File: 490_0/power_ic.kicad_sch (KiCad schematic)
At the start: 35 parts, among them J11 USB3_A_Stacked, U11 TPS2560DRCR, U19 ECMF04-4HSWM10, U20 ECMF04-4HSWM10, U3 TUSB7320RKMR, X2 ECS-480-18-33-JGN-TR

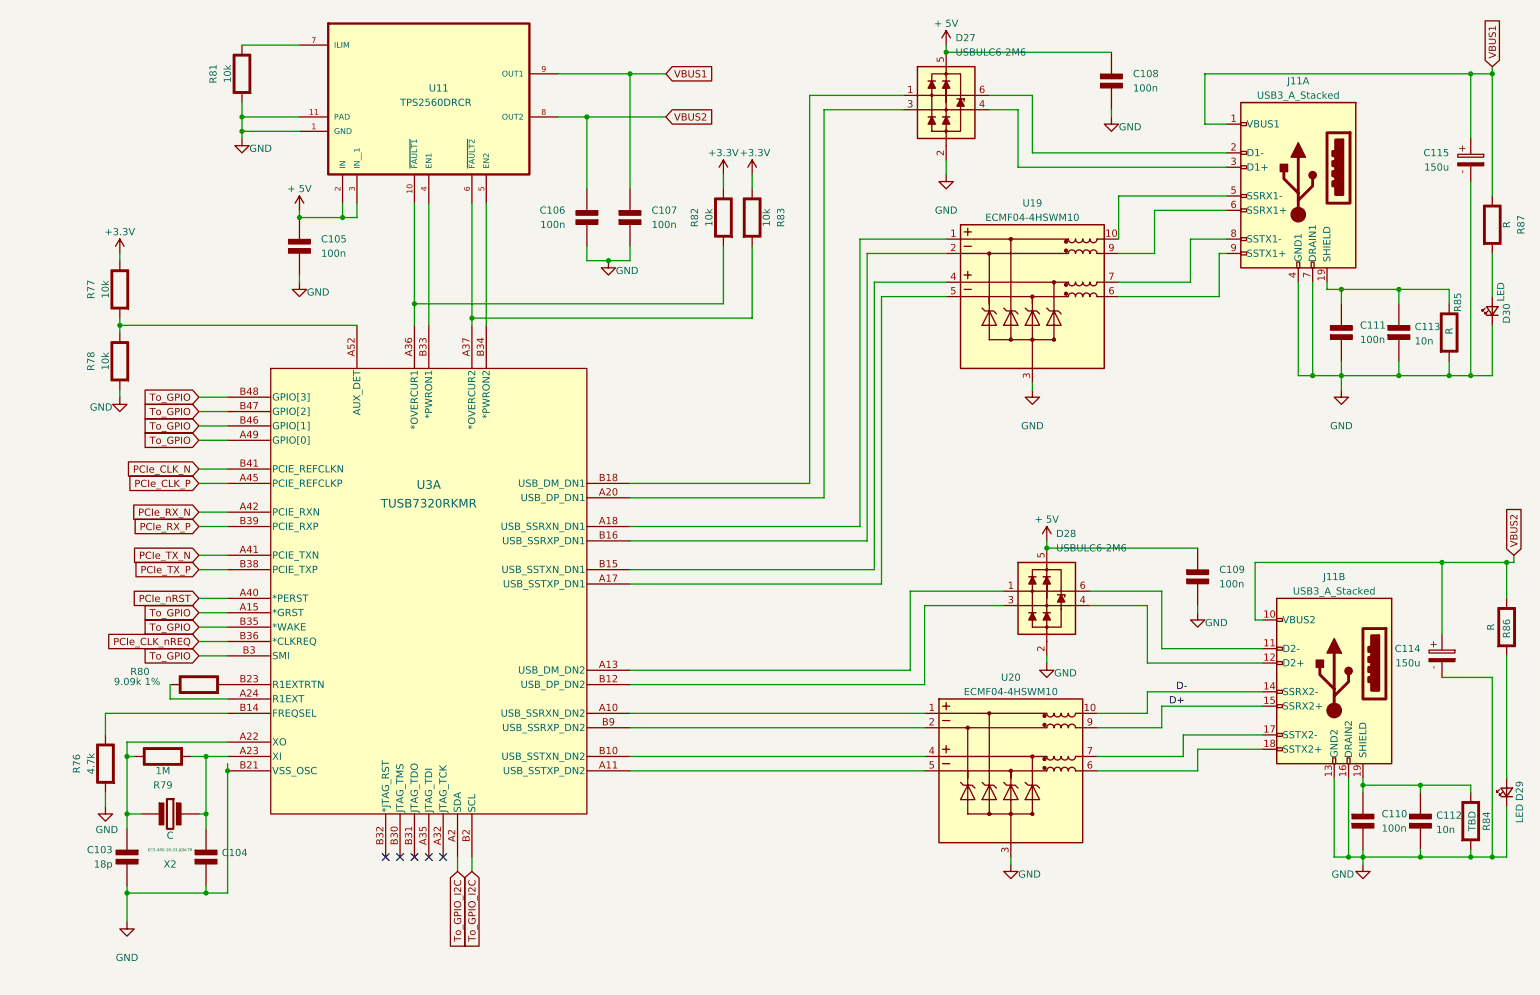
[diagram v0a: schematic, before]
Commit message: US letter format
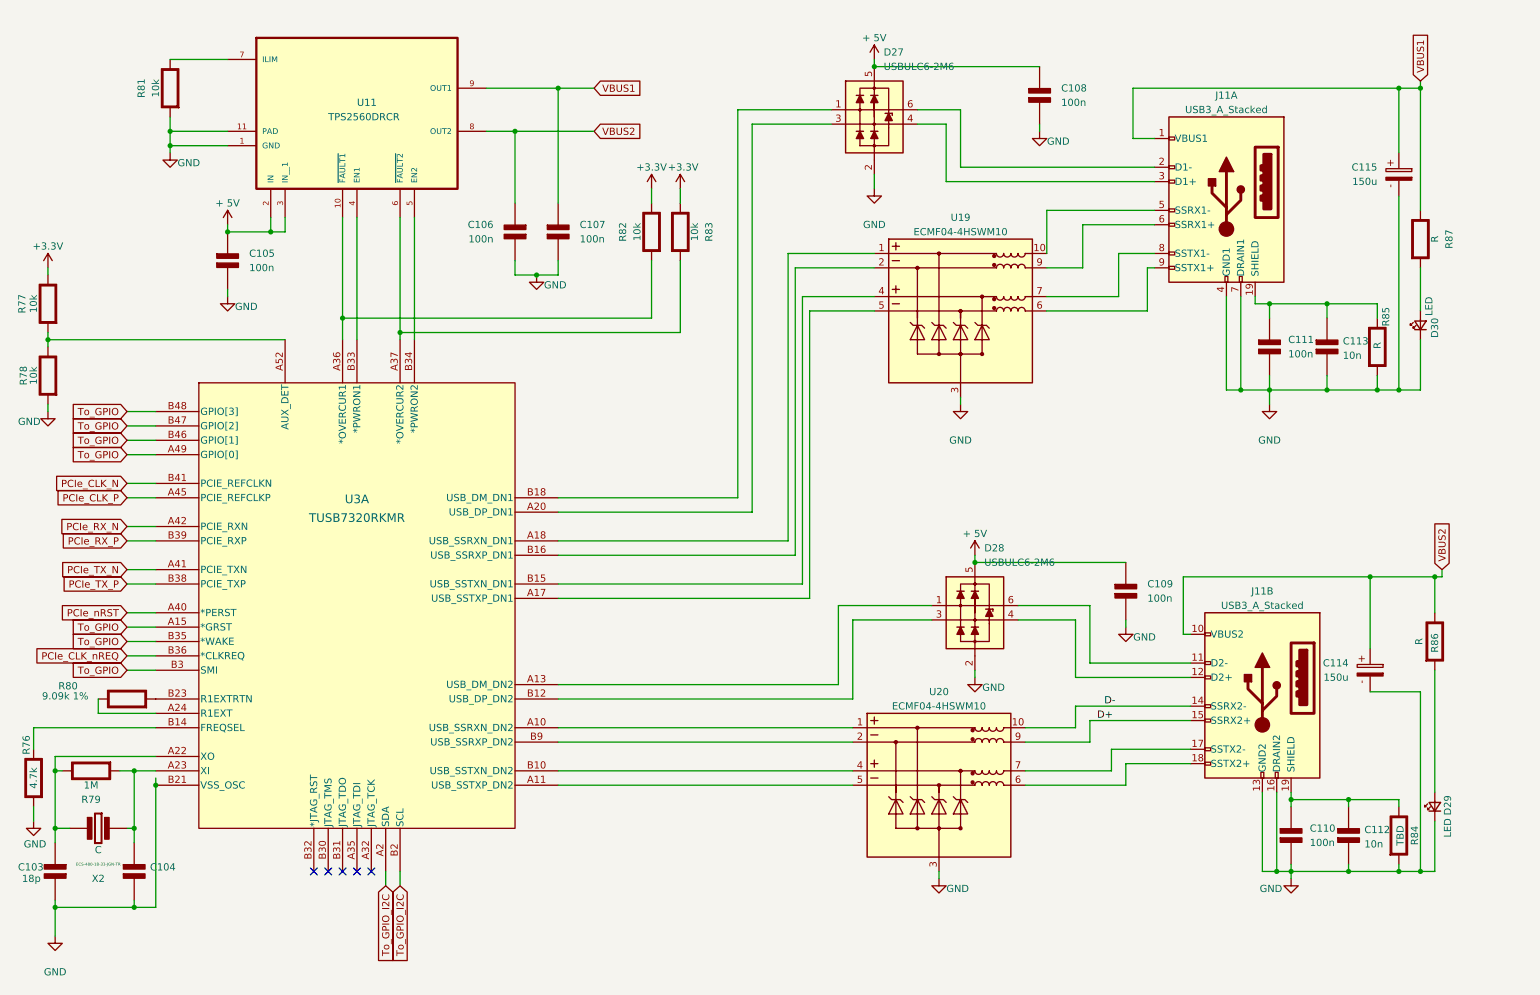
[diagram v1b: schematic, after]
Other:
- moved on the sheet: C103, C104, C105, C106, C107, C108, C109, C110, C111, C112, C113, C114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

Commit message: Changed some local labels to the right format
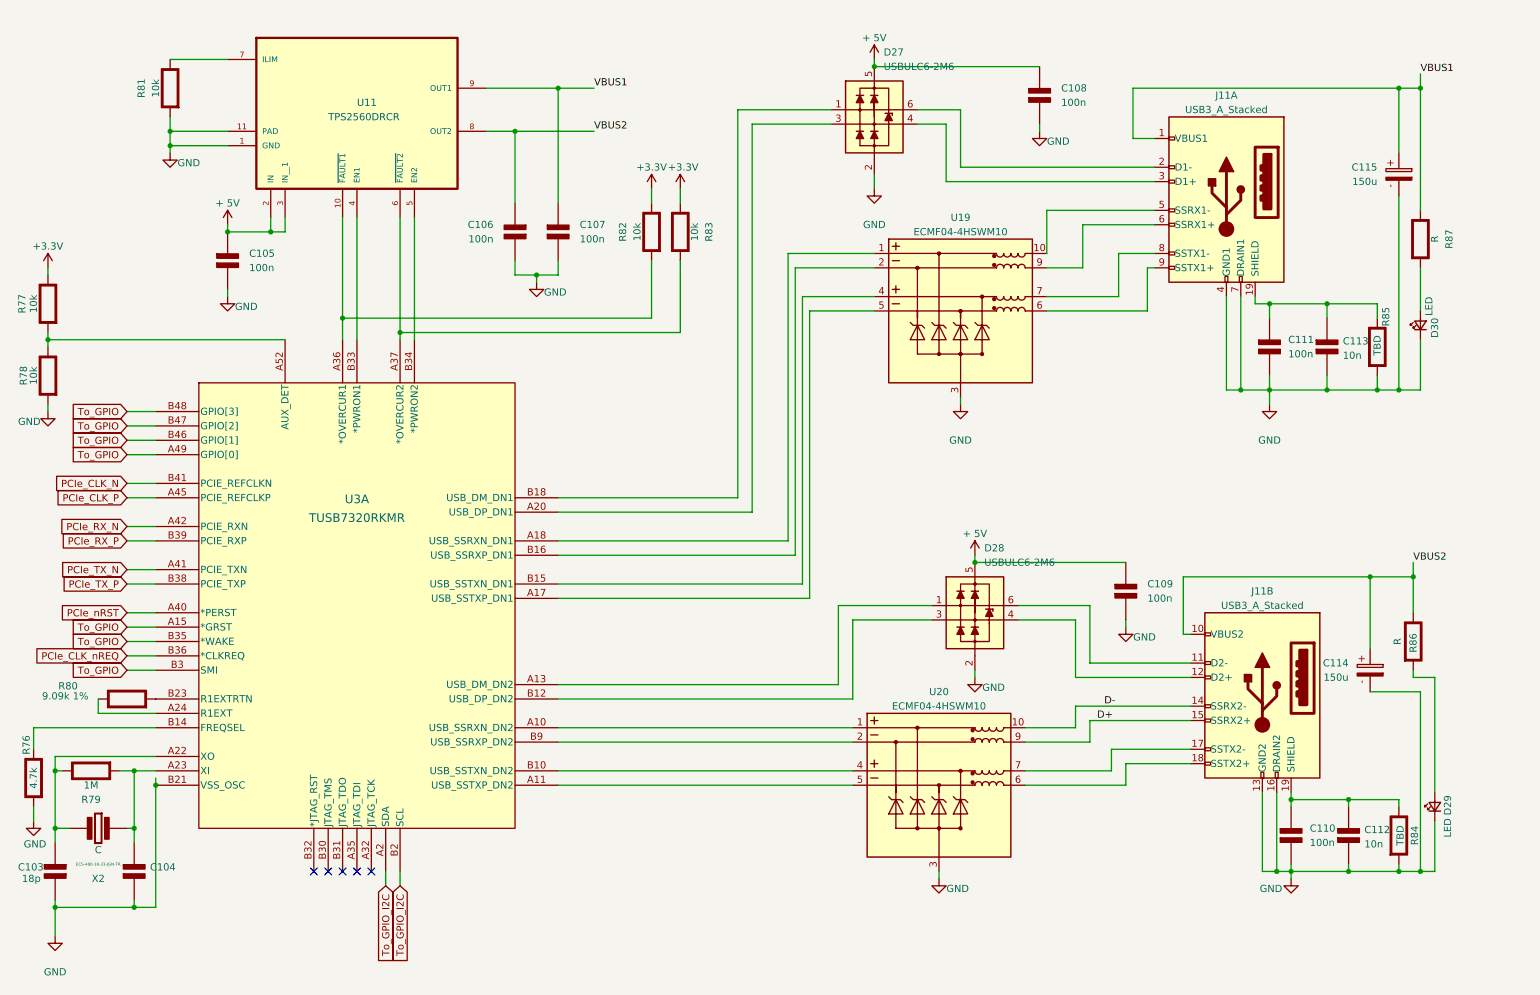
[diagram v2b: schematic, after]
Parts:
- R85: value R -> TBD
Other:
- moved on the sheet: R86
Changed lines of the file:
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@@
 	)
 	(junction
-		(at 262.89 111.76)
+		(at 259.08 111.76)
 		(diameter 0)
 		(color 0 0 0 0)
@@
 	(wire
 		(pts
-			(xy 262.89 128.27) (xy 262.89 149.86)
+			(xy 259.08 128.27) (xy 259.08 129.54)
 		)
 		(stroke
@@
 	(wire
 		(pts
-			(xy 260.35 24.13) (xy 260.35 25.4)
+			(xy 260.35 22.86) (xy 260.35 25.4)
 		)
 		(stroke
@@
 	(wire
 		(pts
-			(xy 251.46 111.76) (xy 262.89 111.76)
+			(xy 251.46 111.76) (xy 259.08 111.76)
 		)
 		(stroke
@@
 	(wire
 		(pts
+			(xy 262.89 129.54) (xy 262.89 149.86)
+		)
+		(stroke
+			(width 0)
+			(type default)
+		)
+	)
+	(wire
+		(pts
 			(xy 15.24 138.43) (xy 36.83 138.43)
 		)
@@
 	(wire
 		(pts
-			(xy 262.89 111.76) (xy 264.16 111.76)
-		)
-		(stroke
-			(width 0)
-			(type default)
-		)
-	)
-	(wire
-		(pts
 			(xy 209.55 25.4) (xy 209.55 34.29)
 		)
@@
 	(wire
 		(pts
-			(xy 226.06 62.23) (xy 226.06 78.74)
+			(xy 259.08 129.54) (xy 262.89 129.54)
 		)
 		(stroke
@@
 	(wire
 		(pts
-			(xy 264.16 110.49) (xy 264.16 111.76)
+			(xy 226.06 62.23) (xy 226.06 78.74)
 		)
 		(stroke
@@
 	(wire
 		(pts
-			(xy 262.89 118.11) (xy 262.89 111.76)
+			(xy 259.08 118.11) (xy 259.08 111.76)
 		)
 		(stroke
@@
 	(wire
 		(pts
+			(xy 104.14 59.69) (xy 104.14 58.42)
+		)
+		(stroke
+			(width 0)
+			(type default)
+		)
+	)
+	(wire
+		(pts
 			(xy 33.02 156.21) (xy 33.02 158.75)
 		)
@@
 	(wire
 		(pts
+			(xy 259.08 109.22) (xy 259.08 111.76)
+		)
+		(stroke
+			(width 0)
+			(type default)
+		)
+	)
+	(wire
+		(pts
 			(xy 100.33 55.88) (xy 100.33 58.42)
 		)
@@
 		)
 	)
+	(label "VBUS1"
+		(at 114.3 25.4 0)
+		(effects
+			(font
+				(size 1.27 1.27)
+			)
+			(justify left bottom)
+		)
+	)
+	(label "VBUS2"
+		(at 114.3 33.02 0)
+		(effects
+			(font
+				(size 1.27 1.27)
+			)
+			(justify left bottom)
+		)
+	)
+	(label "VBUS1"
+		(at 260.35 22.86 0)
+		(effects
+			(font
+				(size 1.27 1.27)
+			)
+			(justify left bottom)
+		)
+	)
+	(label "VBUS2"
+		(at 259.08 109.22 0)
+		(effects
+			(font
+				(size 1.27 1.27)
+			)
+			(justify left bottom)
+		)
+	)
 	(label "D+"
 		(at 203.2 137.16 0)
@@
 		)
 	)
-	(global_label "VBUS2"
-		(shape input)
-		(at 114.3 33.02 0)
-		(fields_autoplaced yes)
-		(effects
-			(font
-				(size 1.27 1.27)
-			)
-			(justify left)
-		)
-		(property "Intersheetrefs" "${INTERSHEET_REFS}"
-			(at 123.3933 33.02 0)
-			(effects
-				(font
-					(size 1.27 1.27)
-				)
-				(justify left)
-				(hide yes)
-			)
-		)
-	)
 	(global_label "To_GPIO"
 		(shape input)
@@
 		)
 	)
-	(global_label "VBUS2"
-		(shape input)
-		(at 264.16 110.49 90)
-		(fields_autoplaced yes)
-		(effects
-			(font
-				(size 1.27 1.27)
-			)
-			(justify left)
-		)
-		(property "Intersheetrefs" "${INTERSHEET_REFS}"
-			(at 264.16 101.3967 90)
-			(effects
-				(font
-					(size 1.27 1.27)
-				)
-				(justify left)
-				(hide yes)
-			)
-		)
-	)
 	(global_label "PCIe_RX_P"
 		(shape input)
@@
 		)
 	)
-	(global_label "VBUS1"
-		(shape input)
-		(at 114.3 25.4 0)
-		(fields_autoplaced yes)
-		(effects
-			(font
-				(size 1.27 1.27)
-			)
-			(justify left)
-		)
-		(property "Intersheetrefs" "${INTERSHEET_REFS}"
-			(at 123.3933 25.4 0)
-			(effects
-				(font
-					(size 1.27 1.27)
-				)
-				(justify left)
-				(hide yes)
-			)
-		)
-	)
 	(global_label "PCIe_RX_N"
 		(shape input)
@@
 		)
 	)
-	(global_label "VBUS1"
-		(shape input)
-		(at 260.35 24.13 90)
-		(fields_autoplaced yes)
-		(effects
-			(font
-				(size 1.27 1.27)
-			)
-			(justify left)
-		)
-		(property "Intersheetrefs" "${INTERSHEET_REFS}"
-			(at 260.35 15.0367 90)
-			(effects
-				(font
-					(size 1.27 1.27)
-				)
-				(justify left)
-				(hide yes)
-			)
-		)
-	)
 	(global_label "PCIe_CLK_P"
 		(shape input)
@@
 	(symbol
 		(lib_id "power:GND")
-		(at 104.14 58.42 0)
+		(at 104.14 59.69 0)
 		(unit 1)
 		(exclude_from_sim no)
@@
 		(dnp no)
 		(property "Reference" "#PWR0223"
-			(at 104.14 64.77 0)
+			(at 104.14 66.04 0)
 			(effects
 				(font
@@
 		)
 		(property "Value" "GND"
-			(at 107.442 60.198 0)
+			(at 107.442 61.468 0)
 			(effects
 				(font
@@
 		)
 		(property "Footprint" ""
-			(at 104.14 58.42 0)
+			(at 104.14 59.69 0)
 			(effects
 				(font
@@
 		)
 		(property "Datasheet" ""
-			(at 104.14 58.42 0)
+			(at 104.14 59.69 0)
 			(effects
 				(font
@@
 		)
 		(property "Description" "Power symbol creates a global label with name \"GND\" , ground"
-			(at 104.14 58.42 0)
+			(at 104.14 59.69 0)
 			(effects
 				(font
@@
 			)
 		)
-		(property "Value" "R"
+		(property "Value" "TBD"
 			(at 252.73 70.866 90)
 			(effects
@@
 	(symbol
 		(lib_id "PCM_Elektuur:R")
-		(at 262.89 123.19 0)
+		(at 259.08 123.19 0)
 		(unit 1)
 		(exclude_from_sim no)
@@
 		(dnp no)
 		(property "Reference" "R86"
-			(at 262.89 123.444 90)
+			(at 259.08 123.444 90)
 			(effects
 				(font
@@
 		)
 		(property "Value" "R"
-			(at 260.096 123.19 90)
+			(at 256.286 123.19 90)
 			(effects
 				(font
@@
 		)
 		(property "Footprint" ""
-			(at 262.89 123.19 0)
+			(at 259.08 123.19 0)
 			(effects
 				(font
@@
 		)
 		(property "Datasheet" ""
-			(at 262.89 123.19 0)
+			(at 259.08 123.19 0)
 			(effects
 				(font
@@
 		)
 		(property "Description" "resistor"
-			(at 262.89 123.19 0)
+			(at 259.08 123.19 0)
 			(effects
 				(font
@@
 		)
 		(property "Indicator" "+"
-			(at 259.715 120.015 0)
+			(at 255.905 120.015 0)
 			(effects
 				(font
@@
 		)
 		(property "Rating" "W"
-			(at 265.43 126.365 0)
+			(at 261.62 126.365 0)
 			(effects
 				(font

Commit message: Fixed buttons
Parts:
- R85: value TBD -> R
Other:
- moved on the sheet: R86
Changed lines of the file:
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@@
 	)
 	(junction
+		(at 262.89 111.76)
+		(diameter 0)
+		(color 0 0 0 0)
+	)
+	(junction
 		(at 33.02 170.18)
 		(diameter 0)
@@
 	)
 	(junction
-		(at 259.08 111.76)
-		(diameter 0)
-		(color 0 0 0 0)
-	)
-	(junction
 		(at 107.95 25.4)
 		(diameter 0)
@@
 	(wire
 		(pts
-			(xy 259.08 128.27) (xy 259.08 129.54)
+			(xy 262.89 128.27) (xy 262.89 149.86)
 		)
 		(stroke
@@
 	(wire
 		(pts
-			(xy 260.35 22.86) (xy 260.35 25.4)
+			(xy 260.35 24.13) (xy 260.35 25.4)
 		)
 		(stroke
@@
 	(wire
 		(pts
-			(xy 251.46 111.76) (xy 259.08 111.76)
+			(xy 251.46 111.76) (xy 262.89 111.76)
 		)
 		(stroke
@@
 	(wire
 		(pts
-			(xy 262.89 129.54) (xy 262.89 149.86)
-		)
-		(stroke
-			(width 0)
-			(type default)
-		)
-	)
-	(wire
-		(pts
 			(xy 15.24 138.43) (xy 36.83 138.43)
 		)
@@
 	(wire
 		(pts
-			(xy 259.08 129.54) (xy 262.89 129.54)
-		)
-		(stroke
-			(width 0)
-			(type default)
-		)
-	)
-	(wire
-		(pts
 			(xy 226.06 62.23) (xy 226.06 78.74)
 		)
@@
 	(wire
 		(pts
-			(xy 259.08 118.11) (xy 259.08 111.76)
+			(xy 262.89 118.11) (xy 262.89 111.76)
 		)
 		(stroke
@@
 	(wire
 		(pts
-			(xy 104.14 59.69) (xy 104.14 58.42)
-		)
-		(stroke
-			(width 0)
-			(type default)
-		)
-	)
-	(wire
-		(pts
 			(xy 33.02 156.21) (xy 33.02 158.75)
 		)
@@
 	(wire
 		(pts
-			(xy 259.08 109.22) (xy 259.08 111.76)
+			(xy 262.89 109.22) (xy 262.89 111.76)
 		)
 		(stroke
@@
 	)
 	(label "VBUS1"
-		(at 260.35 22.86 0)
+		(at 260.35 24.13 0)
 		(effects
 			(font
@@
 	)
 	(label "VBUS2"
-		(at 259.08 109.22 0)
+		(at 262.89 109.22 0)
 		(effects
 			(font
@@
 	(symbol
 		(lib_id "power:GND")
-		(at 104.14 59.69 0)
+		(at 104.14 58.42 0)
 		(unit 1)
 		(exclude_from_sim no)
@@
 		(dnp no)
 		(property "Reference" "#PWR0223"
-			(at 104.14 66.04 0)
+			(at 104.14 64.77 0)
 			(effects
 				(font
@@
 		)
 		(property "Value" "GND"
-			(at 107.442 61.468 0)
+			(at 107.442 60.198 0)
 			(effects
 				(font
@@
 		)
 		(property "Footprint" ""
-			(at 104.14 59.69 0)
+			(at 104.14 58.42 0)
 			(effects
 				(font
@@
 		)
 		(property "Datasheet" ""
-			(at 104.14 59.69 0)
+			(at 104.14 58.42 0)
 			(effects
 				(font
@@
 		)
 		(property "Description" "Power symbol creates a global label with name \"GND\" , ground"
-			(at 104.14 59.69 0)
+			(at 104.14 58.42 0)
 			(effects
 				(font
@@
 			)
 		)
-		(property "Value" "TBD"
+		(property "Value" "R"
 			(at 252.73 70.866 90)
 			(effects
@@
 	(symbol
 		(lib_id "PCM_Elektuur:R")
-		(at 259.08 123.19 0)
+		(at 262.89 123.19 0)
 		(unit 1)
 		(exclude_from_sim no)
@@
 		(dnp no)
 		(property "Reference" "R86"
-			(at 259.08 123.444 90)
+			(at 262.89 123.444 90)
 			(effects
 				(font
@@
 		)
 		(property "Value" "R"
-			(at 256.286 123.19 90)
+			(at 260.096 123.19 90)
 			(effects
 				(font
@@
 		)
 		(property "Footprint" ""
-			(at 259.08 123.19 0)
+			(at 262.89 123.19 0)
 			(effects
 				(font
@@
 		)
 		(property "Datasheet" ""
-			(at 259.08 123.19 0)
+			(at 262.89 123.19 0)
 			(effects
 				(font
@@
 		)
 		(property "Description" "resistor"
-			(at 259.08 123.19 0)
+			(at 262.89 123.19 0)
 			(effects
 				(font
@@
 		)
 		(property "Indicator" "+"
-			(at 255.905 120.015 0)
+			(at 259.715 120.015 0)
 			(effects
 				(font
@@
 		)
 		(property "Rating" "W"
-			(at 261.62 126.365 0)
+			(at 265.43 126.365 0)
 			(effects
 				(font
